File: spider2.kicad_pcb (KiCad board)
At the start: 2 copper layers, 137 x 72.5 mm, 141 parts, among them J1 NRJ6HH, J10 PJ-320A, J11 PJ359, J12 PJ359, J13 PJ359, J14 PJ359, J15 PJ359, J16 PJ359, J17 A, J19 PJ359, J2 NRJ6HH, J20 PJ359, J3 PJ359, J4 PJ359, J5 PJ359, J6 PJ-320A, J7 PJ359, J8 PJ359, J9 PJ359, P1 USB4085, Q1 AOI4286, Q2 BC547, Q3 BC547, SW2 200MDP1T2B2M2QE, SW3 200MDP1T2B2M2QE, SW4 200MDP3T1B1M6QE, U2 AP63203WU, U4 NE5532, U5 MAX4062, U6 MAX4062, U7 PAM8406D

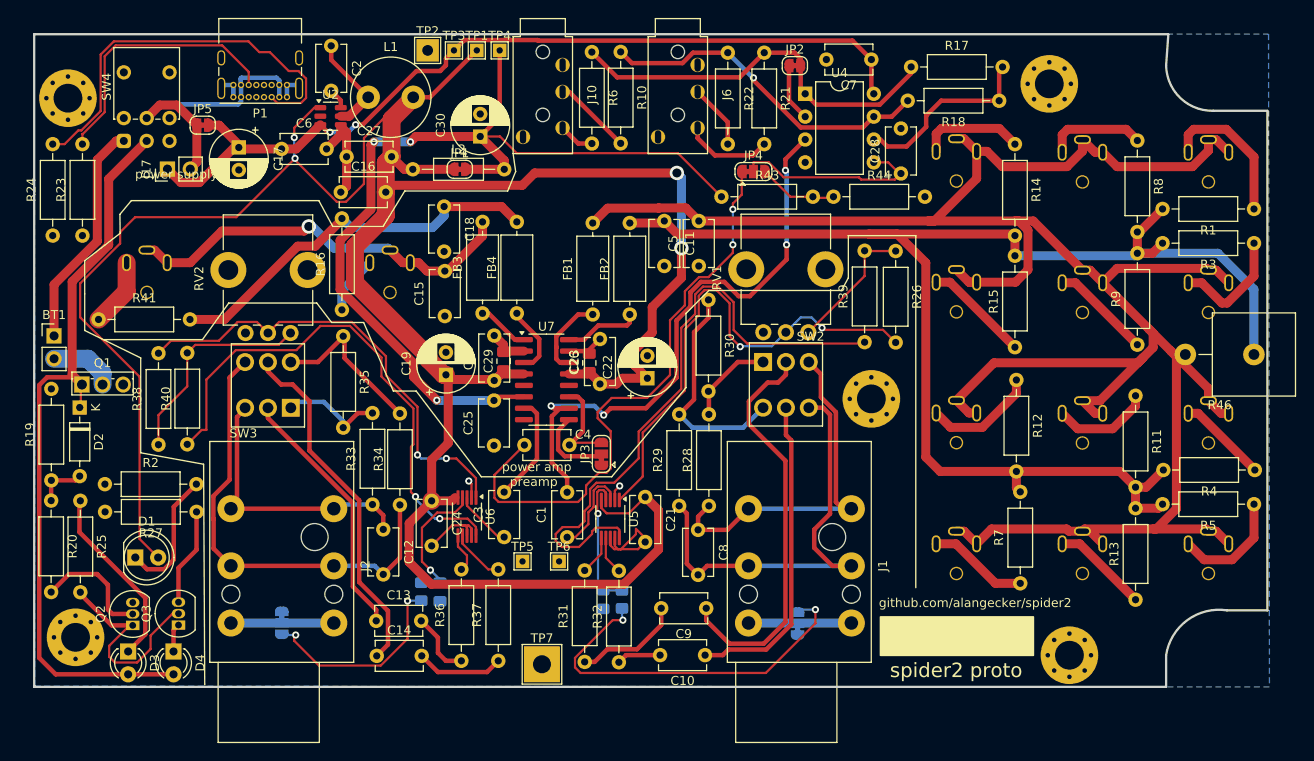
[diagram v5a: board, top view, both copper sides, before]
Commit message: battery LEDs on same position as old on/off switch
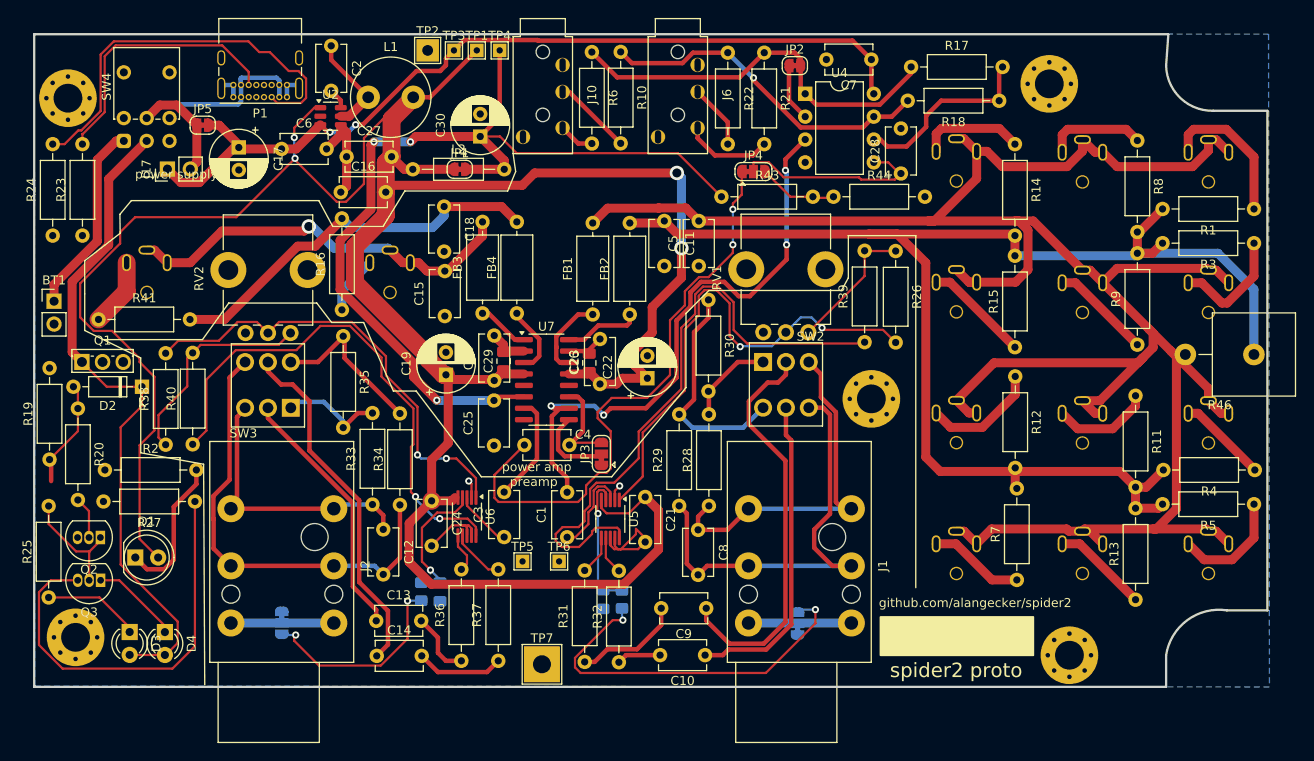
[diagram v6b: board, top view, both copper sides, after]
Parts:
- moved R25 11.3 mm to (139.2, 93.2), turned to 90 degrees
- moved R20 10.7 mm to (142.5, 72.2)
- moved Q2 10.4 mm to (145.0, 86.5), turned to 180 degrees
- moved Q3 9.98 mm to (145.0, 91.2), turned to 180 degrees
- moved D2 7.30 mm to (149.6, 69.8), turned to 180 degrees
- moved BT1 3.85 mm to (139.8, 60.2)
- moved Q1 2.51 mm to (142.9, 67.0)
- moved D4 2.36 mm to (152.2, 97.0)
- moved R19 2.32 mm to (139.3, 77.8)
- moved D3 2.17 mm to (148.2, 97.0)
- moved R2 1.58 mm to (145.5, 79.0)
- moved R27 1.16 mm to (155.5, 82.5)
- moved R38 0.80 mm to (152.2, 76.2)
- moved R40 0.60 mm to (155.2, 76.2)
- moved R7 0.54 mm to (246.8, 91.2)
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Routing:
- net Net-(Q3-E): track 10.9 -> 46.2 mm
- net +BATT: track 85.0 -> 74.3 mm
- net Net-(Q2-C): track 23.3 -> 13.1 mm
- net Net-(D3-K): track 20.6 -> 11.1 mm
- net Net-(Q2-B): track 13.3 -> 4.68 mm
- net Net-(BT1--): track 7.31 -> 0.00 mm
- net Net-(D4-K): track 3.16 -> 10.2 mm
- net Net-(D2-A): track 5.61 -> 12.1 mm
- net Net-(BT1-+): track 25.4 -> 21.5 mm
- net +3.3V: track 292.8 -> 295.4 mm
- net Net-(D1-K): track 14.7 -> 16.3 mm
- net Net-(U6-G2): track 51.4 -> 50.6 mm
- net Net-(U6-G1): track 58.2 -> 57.7 mm
- net Net-(J8-PadS): track 11.2 -> 10.6 mm
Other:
- board text added: "COATI Alis Spider chandi Matthias<3 InterpRise"
- board text added: "originally developed by inspired by new board by with great help of and built by"
- board text removed: "COATI Alis Spider chandi Matthias<3"
- board text removed: "originally developed by inspired by new board by with great help of built by"

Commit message: implement review feedback
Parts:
- removed D3: GREEN, LED_THT:LED_D3.0mm_FlatTop
- removed D4: RED, LED_THT:LED_D3.0mm_FlatTop
- added C33: alt, Capacitor_SMD:C_1210_3225Metric_Pad1.33x2.70mm_HandSolder, F.Cu at (168.6, 43.1)
- added C35: alt, Capacitor_SMD:C_1210_3225Metric_Pad1.33x2.70mm_HandSolder, F.Cu at (174.1, 43.8)
- added C36: alt, Capacitor_SMD:C_1210_3225Metric_Pad1.33x2.70mm_HandSolder, F.Cu at (173.8, 47.8)
- added D5: Red, Green, LED_THT:LED_D5.0mm-3, F.Cu at (147.7, 98.3)
- R30, R35: value 330 -> 330-1%
- R31, R32, R36, R37: value 3.3k-0.1% -> 4.7k-0.1%
- SW2, SW3: value 200MDP1T2B2M2QE -> 200MDP1T2B2M2
- moved L2 13.2 mm to (188.8, 36.0), turned to -90 degrees
- moved R27 10.0 mm to (145.5, 82.5), turned to 0 degrees
- moved JP1 4.54 mm to (188.8, 43.1), turned to -90 degrees
- moved C30 4.11 mm to (183.8, 44.2)
- moved C6 0.42 mm to (165.1, 43.8)
- moved TP5 0.22 mm to (192.1, 89.2)
- moved U2 0.05 mm to (170.6, 39.8)
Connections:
- C21 pad 1: +3.3V -> +3.3VA
- C24 pad 1: +3.3V -> +3.3VA
- U5 pad 5: +3.3V -> +3.3VA
- U6 pad 5: +3.3V -> +3.3VA
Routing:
- net +3.3VA: track 105.7 -> 167.0 mm
- net +3.3V: track 295.4 -> 234.3 mm
- net Net-(U5-G1): track 69.1 -> 40.9 mm, vias 0 -> 2
- net Net-(Q3-E): track 46.2 -> 19.1 mm
- net VCC: track 96.0 -> 106.6 mm
- net Net-(BT1--): track 0.00 -> 7.58 mm
- net +BATT: track 74.3 -> 67.0 mm
- net Net-(D5-K2): track 11.1 -> 18.1 mm
- net /Preamp Floor/OUT: track 6.47 -> 10.1 mm
- net /Preamp Interpreter/OUT: track 10.1 -> 13.2 mm
- net GND: track 59.4 -> 62.3 mm
- net VREF: track 65.6 -> 68.4 mm
- net Net-(D5-K1): track 10.2 -> 8.15 mm
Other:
- board text added: "+"

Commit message: beautiful silkscreen design
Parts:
- L1: value 4.7uH, >2A, <100mOhm -> 4.7uH, >2A
- U2: value AP63203WU -> AP63203
- moved L2 1.25 mm to (188.8, 37.2)
- moved C14 0.85 mm to (175.7, 100.5)
- moved R17 0.60 mm to (234.6, 34.6)
- moved C28 0.19 mm to (233.8, 46.0)
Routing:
- net +3.3V: track 234.3 -> 245.1 mm
- net +BATT: track 67.0 -> 71.3 mm
- net GND: track 62.3 -> 65.4 mm, vias 2 -> 3
- net /Preamp Floor/BIAS: track 23.0 -> 24.8 mm
- net +3.3VA: track 167.0 -> 168.8 mm
- net VREF: track 68.4 -> 69.5 mm
- net Net-(SW3B-B): track 39.4 -> 40.3 mm
- net Net-(SW4B-C): track 17.0 -> 17.6 mm
- net Net-(JP2-B): track 44.3 -> 43.7 mm
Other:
- board text added: "spider chain"
